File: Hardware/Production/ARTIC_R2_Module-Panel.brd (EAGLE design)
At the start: 154.2 x 147.3 mm, 2846 parts, among them J101 U.FL, J126 U.FL, J151 U.FL, J176 U.FL, J201 U.FL, J226 U.FL, J25 U.FL, J251 U.FL, J26 U.FL, J276 U.FL, J301 U.FL, J326 U.FL, J351 U.FL, J376 U.FL, J401 U.FL, J426 U.FL, J451 U.FL, J476 U.FL, J51 U.FL, J76 U.FL, K1 TLP3475R, K10 TLP3475R, K11 TLP3475R, K12 TLP3475R, K13 TLP3475R, K14 TLP3475R, K15 TLP3475R, K16 TLP3475R, K17 TLP3475R, K18 TLP3475R, K19 TLP3475R, K2 TLP3475R, K20 TLP3475R, K3 TLP3475R, K4 TLP3475R, K5 TLP3475R, K6 TLP3475R, K7 TLP3475R, K8 TLP3475R, K9 TLP3475R, Q1 5.8A/30V/35mΩ, Q10 5.8A/30V/35mΩ, Q11 5.8A/30V/35mΩ, Q12 5.8A/30V/35mΩ, Q13 5.8A/30V/35mΩ, Q14 5.8A/30V/35mΩ, Q15 5.8A/30V/35mΩ, Q16 5.8A/30V/35mΩ, Q17 5.8A/30V/35mΩ, Q18 5.8A/30V/35mΩ, Q19 5.8A/30V/35mΩ, Q2 5.8A/30V/35mΩ, Q20 5.8A/30V/35mΩ, Q3 5.8A/30V/35mΩ, Q4 5.8A/30V/35mΩ, Q5 5.8A/30V/35mΩ, Q6 5.8A/30V/35mΩ, Q7 5.8A/30V/35mΩ, Q8 5.8A/30V/35mΩ, Q9 5.8A/30V/35mΩ, U1 ADM4210-1, U10 1.8V/100mA, U100 1.8V/100mA, U101 3.0V, U102 ADM4210-1, U103 ARTIC_R2, U104 RFPA0133, U105 AS179-92LF, U106 1.8V/100mA, U107 3.0V, U108 ADM4210-1, U109 ARTIC_R2, U11 3.0V, U110 RFPA0133, U111 AS179-92LF, U112 1.8V/100mA, U113 3.0V, U114 ADM4210-1, U115 ARTIC_R2, U116 RFPA0133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

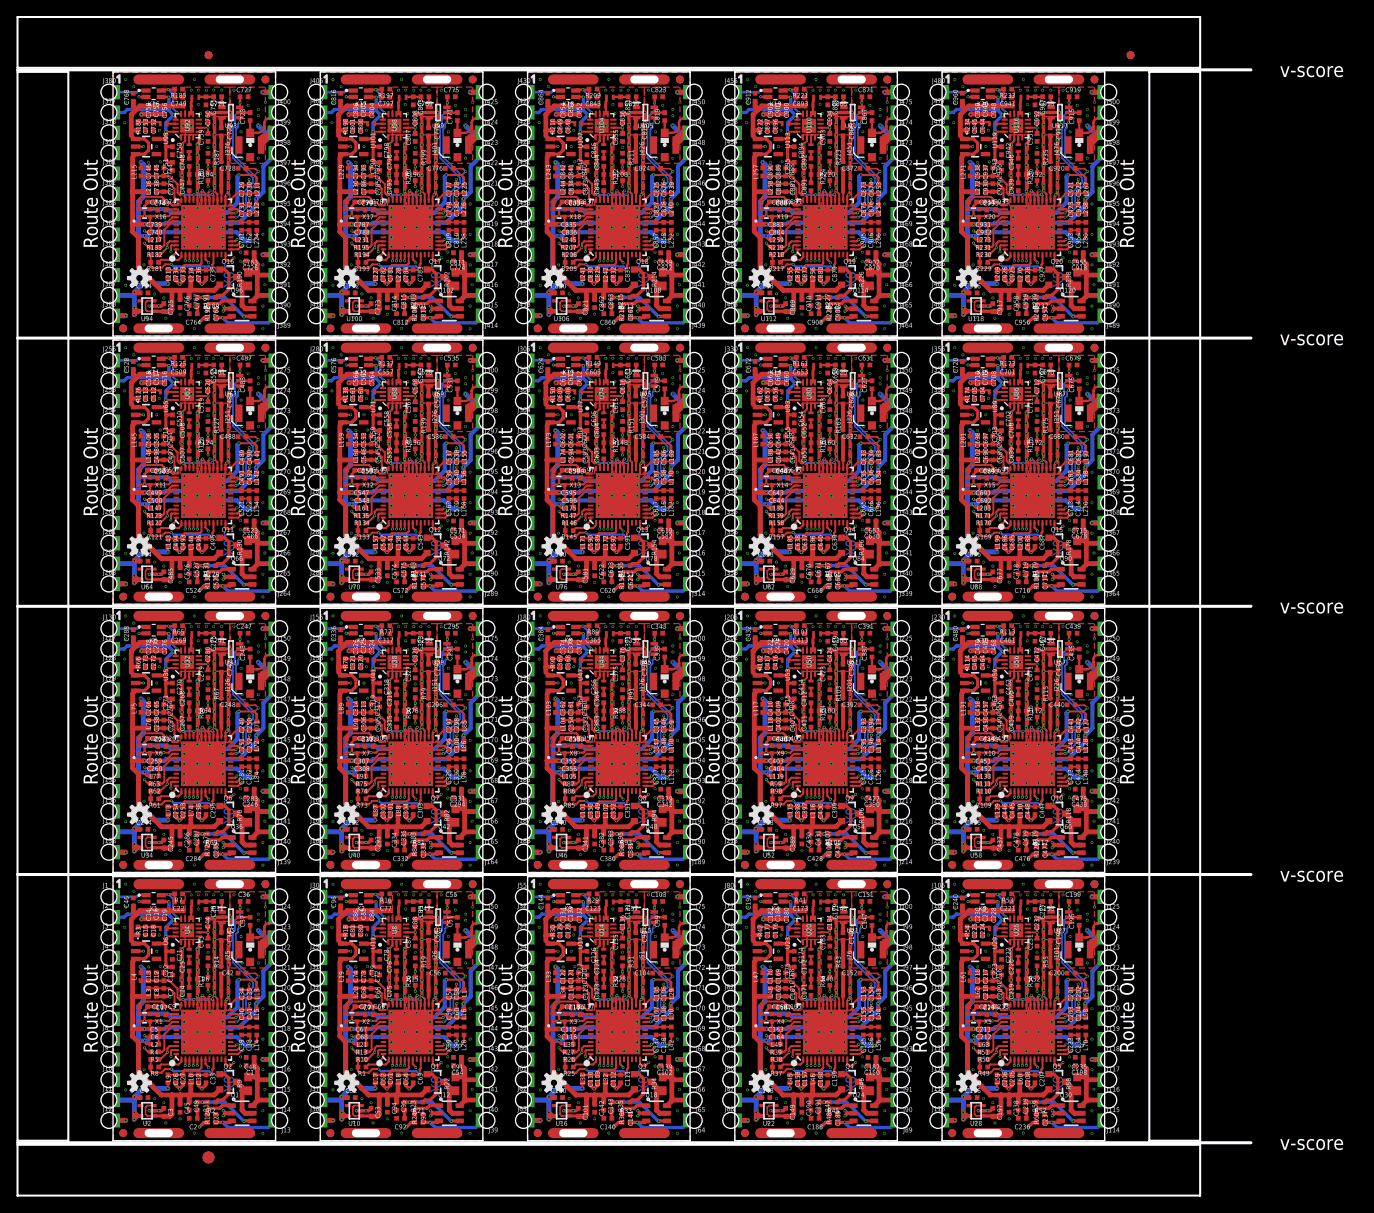
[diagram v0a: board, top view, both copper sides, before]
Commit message: Added the flash memory in USON format
The flash has its own power pin so it can be programmed independantly - without needing the ARTIC to be powered up and held in reset. The user will need to jump the flash power pad across to the adjacent VDD pad on their board.
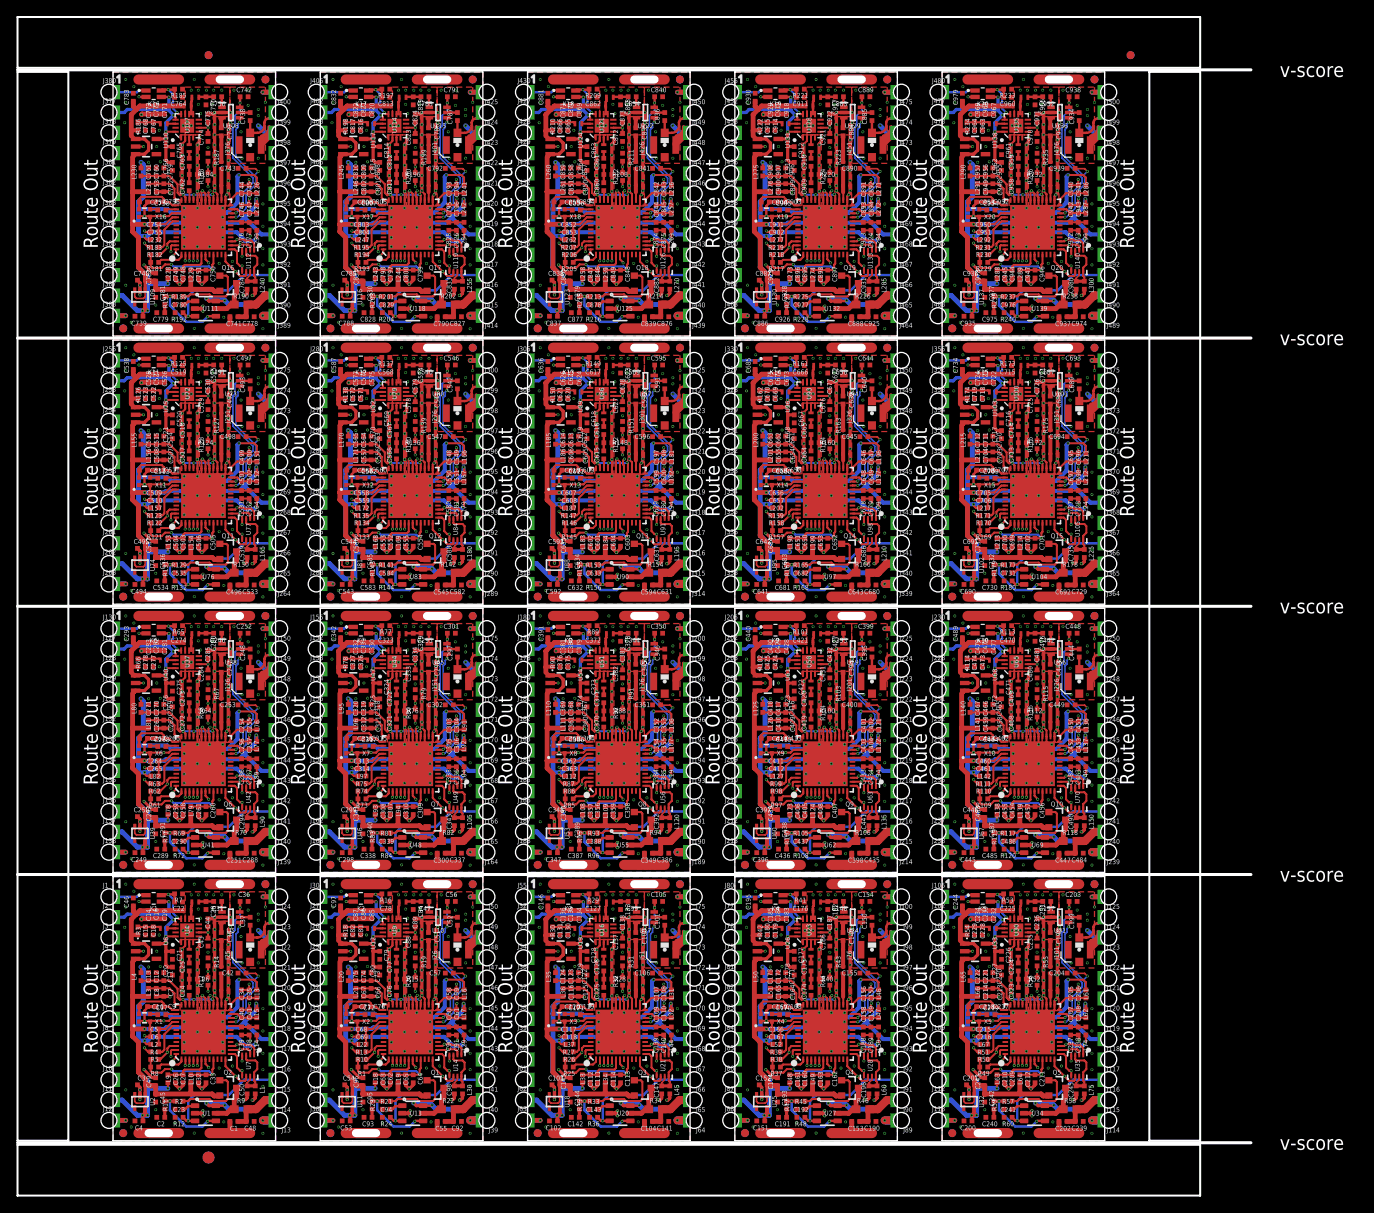
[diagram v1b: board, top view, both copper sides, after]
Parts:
- removed LOGO21, LOGO22, LOGO23, LOGO24, LOGO25, LOGO26, LOGO27, LOGO28, LOGO29, LOGO30, LOGO31, LOGO32, LOGO33, LOGO34, LOGO35, LOGO36, LOGO37, LOGO38, LOGO39, LOGO40: OSHW-LOGOS, SparkFun-Aesthetics:OSHW-LOGO-S
- added C961, C967, C970: 100pF, SparkFun-Capacitors:0402-TIGHT
- added C962, C964, C968, C971, C977: 2.2uF, SparkFun-Capacitors:0402-TIGHT
- added C963, C972: 22pF, SparkFun-Capacitors:0402-TIGHT
- added C965: 2.4 pF, SparkFun-Capacitors:0402_MURATA
- added C966: 9.1pF, New_Parts_Capacitors:0402-TIGHT
- added C969: 10uF, SparkFun-Capacitors:0402-TIGHT
- added C973, C974, C978, C980: 0.1uF, SparkFun-Capacitors:0402-TIGHT
- added C975: 10nF, SparkFun-Capacitors:0402-TIGHT
- added C976, C979: 1.0uF, SparkFun-Capacitors:0402-TIGHT
- added L281, L296: 12nH, New_Parts_Coils:0402_COILCRAFT
- added L282, L297: 30nH, New_Parts_Coils:0402_COILCRAFT
- added L283, L298: 51nH, New_Parts_Coils:0402_COILCRAFT
- added L284, L285, L286, L287, L288, L289, L290, L291, L292, L299, L300: 30Ω, SparkFun-Coils:0402-TIGHT
- added L293: 18nH, New_Parts_Coils:0402_COILCRAFT
- added L294: 15nH, New_Parts_Coils:0402_COILCRAFT
- added L295: 27nH, New_Parts_Coils:0402_COILCRAFT
- added U121, U128, U135: RFPA0133, New_Parts_IC-Comms:QFN50P300X300X86-17N
- added U122, U129, U136: AS179-92LF, New_Parts_IC-Comms:SOT65P220X100-6N
- added U123, U130, U137: 1.8V/100mA, SparkFun-IC-Power:SC70
- added U124, U131, U138: 3.0V, New_Parts_IC-Power:SOT23-5
- added U125, U132, U139: ADM4210-1, New_Parts_IC-Power:TSOT6
- added U126, U133, U140: SST25VF020BUSON, New_Parts_IC-Memory:USON_3X2MM
- added U127, U134: ARTIC_R2, New_Parts_IC-Comms:QFN-48
- C100, C101, C148, C149, C197, C333, C477, C480, C52, C624, C645, C676, C693, C725, C73, C765, C813, C820, C841, C861, C869, C885, C889, C909, C912, C933, C960: value 1.0uF -> 100pF
- C102, C319, C342, C417, C486, C511, C54, C609, C613, C760, C805, C94, C952: value 2.2uF -> 1.0uF
- C103, C123, C146, C151, C152, C168, C172, C195, C200, C221, C241, C270, C290, C315, C339, C364, C391, C413, C440, C462, C535, C564, C584, C711, C756, C903, C936, C97: value 100pF -> 1.0uF
- C104, C135, C180, C193, C242, C276, C291, C327, C423, C481, C487, C530, C536, C55, C579, C625, C674, C723, C775, C817, C824, C866, C888, C913, C915, C919: value 100pF -> 2.2uF
- C105, C128, C137, C155, C176, C203, C224, C253, C272, C281, C297, C301, C345, C351, C393, C395, C399, C416, C443, C449, C491, C493, C497, C541, C547, C569, C57, C589, C591, C595, C617, C639, C665, C687, C689, C713, C737, C785, C787, C835, C857, C883, C921: value 22pF -> 100pF
- C106, C154, C186, C204, C235, C252, C302, C330, C346, C350, C379, C394, C400, C431, C442, C444, C448, C492, C498, C540, C542, C546, C575, C590, C596, C618, C638, C640, C644, C666, C667, C688, C714, C715, C736, C738, C762, C763, C786, C811, C834, C836, C863, C884, C906, C911, C932, C955, C959: value 0.1uF -> 100pF
- C117, C213, C237, C309, C313, C384, C405, C409, C501, C505, C580, C597, C601, C629, C669, C697, C793, C816: value 1.0uF -> 22pF
- C118, C214, C310, C406, C502, C598: value 47nF -> 0.1uF
- C119, C887, C935: value 1.0nF -> 1.0uF
- C120, C267, C316, C365, C414, C708, C855: value 100pF -> 47nF
- C121: value 1.0uF -> 1.0nF
- C122, C134, C422, C470, C518, C566, C710, C890, C938: value 10uF -> 100pF
- C124, C173, C222, C516, C577, C626, C663, C675, C75, C87, C871, C920: value 100pF -> 10uF
- C127, C150, C175, C177, C198, C223, C225, C232, C246, C273, C321, C367, C373, C382, C421, C465, C469, C517, C520, C526, C568, C616, C661, C664, C774, C79, C808, C814, C85, C862, C88, C910, C918, C958: value 2.2uF -> 100pF
- C130, C754, C850, C946: value 2.4 pF -> 22pF; device SparkFun-Capacitors:0402_MURATA -> SparkFun-Capacitors:0402-TIGHT
- C131, C227: value 9.1pF -> 2.2uF; device New_Parts_Capacitors:0402-TIGHT -> SparkFun-Capacitors:0402-TIGHT
- C132, C279, C769, C818, C867: value 100pF -> 2.4 pF; device SparkFun-Capacitors:0402-TIGHT -> SparkFun-Capacitors:0402_MURATA
- C133, C280, C574: value 2.2uF -> 9.1pF; device SparkFun-Capacitors:0402-TIGHT -> New_Parts_Capacitors:0402-TIGHT
- C136, C271, C369, C430, C565, C712, C822: value 2.2uF -> 10uF
- C138, C187, C202, C282, C300, C331, C383, C398, C474, C496, C523, C527, C570, C594, C619, C634, C692, C719, C732, C815, C830, C922, C928, C95: value 0.1uF -> 2.2uF
- C139, C156, C158, C160, C162, C164, C254, C256, C258, C260, C335, C352, C354, C356, C450, C452, C522, C548, C571, C58, C60, C62, C64, C66, C68, C767, C874, C90: value 0.1uF -> 22pF
- C140, C92: value 10nF -> 0.1uF
- C141, C165, C189, C196, C245, C261, C265, C288, C292, C336, C341, C357, C361, C453, C457, C484, C532, C533, C549, C553, C581, C649, C69, C745, C96: value 1.0uF -> 0.1uF
- C142, C534: value 2.2uF -> 10nF
- C143, C250, C298, C348, C396, C446, C494, C538, C544, C592, C636, C642, C682, C690, C734, C740, C780, C788, C832, C858, C878, C907, C930: value 0.1uF -> 1.0uF
- C144, C285, C340, C389, C429, C432, C576, C621, C628, C677, C717, C741, C768, C772, C821, C864, C937: value 1.0uF -> 2.2uF
- C145, C147, C194, C216, C243, C312, C337, C343, C363, C385, C386, C392, C408, C412, C434, C435, C439, C459, C461, C483, C488, C50, C504, C508, C510, C555, C557, C600, C604, C606, C631, C651, C653, C679, C680, C696, C700, C702, C728, C747, C749, C796, C798, C804, C843, C845, C892, C894, C900, C941, C951, C98: value 100pF -> 0.1uF
- C153, C233, C251, C349, C425, C447, C521, C545, C585, C643, C683, C781, C80, C873, C879, C89: value 22pF -> 2.2uF
- C157, C159, C161, C163, C255, C257, C259, C353, C355, C441, C451, C537, C539, C59, C608, C61, C63, C635, C637, C65, C67, C704, C729, C733, C735, C777, C800, C827, C831, C833, C875, C896, C925, C929, C931: value 22pF -> 0.1uF
- C166, C262, C358, C454, C550, C646: value 47nF -> 22pF
- C167, C263, C359, C455, C551, C647: value 1.0nF -> 0.1uF
- C169: value 1.0uF -> 47nF
- C170, C758: value 10uF -> 1.0nF
- C178, C82: value 2.4 pF -> 2.2uF; device SparkFun-Capacitors:0402_MURATA -> SparkFun-Capacitors:0402-TIGHT
- C179, C803, C899: value 9.1pF -> 22pF; device New_Parts_Capacitors:0402-TIGHT -> SparkFun-Capacitors:0402-TIGHT
- C181, C328, C622: value 2.2uF -> 2.4 pF; device SparkFun-Capacitors:0402-TIGHT -> SparkFun-Capacitors:0402_MURATA
- C182: value 10uF -> 9.1pF; device SparkFun-Capacitors:0402-TIGHT -> New_Parts_Capacitors:0402-TIGHT
- C185, C320, C761: value 22pF -> 10uF
- C188, C620: value 10nF -> 22pF
- C190, C238, C294, C390, C559, C582, C630, C655, C657, C751, C753, C847, C849, C853, C943, C945, C949: value 2.2uF -> 0.1uF
- C191, C730, C828, C926: value 0.1uF -> 10nF
- C201, C249, C299, C347, C368, C397, C445, C489, C495, C543, C560, C587, C593, C633, C641, C685, C691, C731, C739, C783, C809, C829, C881, C927: value 22pF -> 1.0uF
- C215, C311, C407, C503, C599, C695: value 1.0nF -> 22pF
- C218, C806: value 10uF -> 47nF
- C219, C268, C317, C366, C660, C72, C807: value 100pF -> 1.0nF
- C226, C274, C322, C370, C514: value 2.4 pF -> 100pF; device SparkFun-Capacitors:0402_MURATA -> SparkFun-Capacitors:0402-TIGHT
- C228, C264, C360, C375, C411, C433, C456, C460, C482, C507, C509, C531, C552, C556, C558, C603, C605, C648, C652, C654, C699, C701, C727, C744, C748, C750, C776, C795, C797, C844, C846, C852, C865, C891, C893, C914, C940, C942, C948: value 100pF -> 22pF
- C230: value 10uF -> 2.4 pF; device SparkFun-Capacitors:0402-TIGHT -> SparkFun-Capacitors:0402_MURATA
- C231, C721, C770, C819, C84: value 100pF -> 9.1pF; device SparkFun-Capacitors:0402-TIGHT -> New_Parts_Capacitors:0402-TIGHT
- C234, C283, C479, C810, C859: value 0.1uF -> 10uF
- C236, C380, C572, C668: value 10nF -> 2.2uF
- C240, C436, C485, C93: value 1.0uF -> 10nF
- C266, C662, C74, C854: value 10uF -> 1.0uF
- C275, C323, C371, C419, C563: value 9.1pF -> 100pF; device New_Parts_Capacitors:0402-TIGHT -> SparkFun-Capacitors:0402-TIGHT
- C277, C286, C424, C607, C678, C703, C705, C718, C799, C801, C81, C895, C897, C901: value 2.2uF -> 22pF
- C278, C374, C86: value 10uF -> 2.2uF
- C284, C428, C716, C764, C812, C860: value 10nF -> 100pF
- C289, C338, C387, C583, C632: value 100pF -> 10nF
- C314, C410, C506, C602, C698, C794, C902: value 10uF -> 0.1uF
- C326, C362, C458, C554, C650, C746, C842, C950: value 10uF -> 22pF
- C329: value 22pF -> 9.1pF; device SparkFun-Capacitors:0402-TIGHT -> New_Parts_Capacitors:0402-TIGHT
- C332, C908: value 10nF -> 10uF
- C377: value 22pF -> 2.4 pF; device SparkFun-Capacitors:0402-TIGHT -> SparkFun-Capacitors:0402_MURATA
- C378, C427, C623: value 0.1uF -> 9.1pF; device SparkFun-Capacitors:0402-TIGHT -> New_Parts_Capacitors:0402-TIGHT
- C381, C528, C724, C773, C957: value 1.0uF -> 10uF
- C415, C513, C709, C856: value 2.2uF -> 1.0nF
- C418: value 2.4 pF -> 10uF; device SparkFun-Capacitors:0402_MURATA -> SparkFun-Capacitors:0402-TIGHT
- C426, C475, C671: value 0.1uF -> 2.4 pF; device SparkFun-Capacitors:0402-TIGHT -> SparkFun-Capacitors:0402_MURATA
- C463, C561, C757, C904: value 2.2uF -> 47nF
- C464, C905: value 22pF -> 1.0nF
- C466, C658: value 2.4 pF -> 1.0uF; device SparkFun-Capacitors:0402_MURATA -> SparkFun-Capacitors:0402-TIGHT
- C467: value 9.1pF -> 10uF; device New_Parts_Capacitors:0402-TIGHT -> SparkFun-Capacitors:0402-TIGHT
- C476: value 10nF -> 9.1pF; device SparkFun-Capacitors:0402-TIGHT -> New_Parts_Capacitors:0402-TIGHT
- C512, C953: value 22pF -> 47nF
- C515, C707: value 9.1pF -> 1.0uF; device New_Parts_Capacitors:0402-TIGHT -> SparkFun-Capacitors:0402-TIGHT
- C524: value 10nF -> 2.4 pF; device SparkFun-Capacitors:0402-TIGHT -> SparkFun-Capacitors:0402_MURATA
- C525, C672, C868, C917: value 1.0uF -> 9.1pF; device SparkFun-Capacitors:0402-TIGHT -> New_Parts_Capacitors:0402-TIGHT
- C562: value 2.4 pF -> 1.0nF; device SparkFun-Capacitors:0402_MURATA -> SparkFun-Capacitors:0402-TIGHT
- C573, C720, C916: value 1.0uF -> 2.4 pF; device SparkFun-Capacitors:0402-TIGHT -> SparkFun-Capacitors:0402_MURATA
- C610: value 2.4 pF -> 47nF; device SparkFun-Capacitors:0402_MURATA -> SparkFun-Capacitors:0402-TIGHT
- C611: value 9.1pF -> 1.0nF; device New_Parts_Capacitors:0402-TIGHT -> SparkFun-Capacitors:0402-TIGHT
- C659: value 9.1pF -> 47nF; device New_Parts_Capacitors:0402-TIGHT -> SparkFun-Capacitors:0402-TIGHT
- C681, C779, C877: value 22pF -> 10nF
- C694, C742, C934: value 47nF -> 100pF
- C70, C838, C886: value 47nF -> 1.0uF
- C706, C802, C898: value 2.4 pF -> 0.1uF; device SparkFun-Capacitors:0402_MURATA -> SparkFun-Capacitors:0402-TIGHT
- C71: value 1.0nF -> 47nF
- C743, C791: value 1.0nF -> 100pF
- C755, C851, C947: value 9.1pF -> 0.1uF; device New_Parts_Capacitors:0402-TIGHT -> SparkFun-Capacitors:0402-TIGHT
- C790: value 47nF -> 2.2uF
- C83: value 9.1pF -> 2.4 pF; device New_Parts_Capacitors:0402-TIGHT -> SparkFun-Capacitors:0402_MURATA
- C839: value 1.0nF -> 2.2uF
- C954: value 0.1uF -> 1.0nF
- C956: value 10nF -> 1.0uF
- L100, L115, L130, L145, L160, L175, L280, L70, L85: value 30Ω -> 27nH; device SparkFun-Coils:0402-TIGHT -> New_Parts_Coils:0402_COILCRAFT
- L101, L116, L131, L146, L161, L266, L56, L71, L86: value 30Ω -> 12nH; device SparkFun-Coils:0402-TIGHT -> New_Parts_Coils:0402_COILCRAFT
- L102, L117, L132, L147, L252, L267, L42, L57, L72, L87: value 30Ω -> 30nH; device SparkFun-Coils:0402-TIGHT -> New_Parts_Coils:0402_COILCRAFT
- L103, L118, L133, L238, L253, L268, L28, L43, L58, L73, L88: value 30Ω -> 51nH; device SparkFun-Coils:0402-TIGHT -> New_Parts_Coils:0402_COILCRAFT
- L106, L120, L134, L22, L232, L246, L260, L274, L36, L50, L64, L78, L92: value 18nH -> 30Ω; device New_Parts_Coils:0402_COILCRAFT -> SparkFun-Coils:0402-TIGHT
- L107, L121, L135, L149, L247, L261, L275, L37, L51, L65, L79, L93: value 15nH -> 30Ω; device New_Parts_Coils:0402_COILCRAFT -> SparkFun-Coils:0402-TIGHT
- L108, L122, L136, L150, L164, L262, L276, L52, L66, L80, L94: value 27nH -> 30Ω; device New_Parts_Coils:0402_COILCRAFT -> SparkFun-Coils:0402-TIGHT
- L109, L123, L137, L151, L165, L179, L277, L67, L81, L95: value 12nH -> 30Ω; device New_Parts_Coils:0402_COILCRAFT -> SparkFun-Coils:0402-TIGHT
- L110, L124, L138, L152, L166, L180, L194, L82, L96: value 30nH -> 30Ω; device New_Parts_Coils:0402_COILCRAFT -> SparkFun-Coils:0402-TIGHT
- L111, L125, L139, L153, L167, L181, L195, L209, L97: value 51nH -> 30Ω; device New_Parts_Coils:0402_COILCRAFT -> SparkFun-Coils:0402-TIGHT
- L113, L128, L143, L158, L173, L188, L203, L98: value 30Ω -> 18nH; device SparkFun-Coils:0402-TIGHT -> New_Parts_Coils:0402_COILCRAFT
- L114, L129, L144, L159, L174, L189, L84, L99: value 30Ω -> 15nH; device SparkFun-Coils:0402-TIGHT -> New_Parts_Coils:0402_COILCRAFT
- L148: value 18nH -> 51nH
- L162: value 18nH -> 30nH
- L163: value 15nH -> 51nH
- L176: value 18nH -> 12nH
- L177: value 15nH -> 30nH
- L178: value 27nH -> 51nH
- L190: value 18nH -> 27nH
- L191: value 15nH -> 12nH
- L192: value 27nH -> 30nH
- L193: value 12nH -> 51nH
- L204: value 18nH -> 15nH
- L205: value 15nH -> 27nH
- L206: value 27nH -> 12nH
- L207: value 12nH -> 30nH
- L208: value 30nH -> 51nH
- L23, L233: value 15nH -> 18nH
- L234, L24: value 27nH -> 15nH
- L235, L25: value 12nH -> 27nH
- L236, L26: value 30nH -> 12nH
- L237, L27: value 51nH -> 30nH
- L248, L38: value 27nH -> 18nH
- L249, L39: value 12nH -> 15nH
- L250, L40: value 30nH -> 27nH
- L251, L41: value 51nH -> 12nH
- L263, L53: value 12nH -> 18nH
- L264, L54: value 30nH -> 15nH
- L265, L55: value 51nH -> 27nH
- L278, L68: value 30nH -> 18nH
- L279, L69: value 51nH -> 15nH
- L83: value 51nH -> 18nH
- U$100, U$126, U$152, U$178, U$204, U$230, U$256, U$282, U$308, U$334, U$360, U$386, U$412, U$438, U$464, U$48, U$490, U$516, U$74: device output:#SCLK#0 -> output:#COPI#0
- U$101, U$127, U$153, U$179, U$205, U$231, U$257, U$283, U$309, U$335, U$361, U$387, U$413, U$439, U$465, U$49, U$491, U$517, U$75: device output:#COPI#0 -> output:#CIPO#0
- U$102, U$128, U$154, U$180, U$206, U$232, U$258, U$284, U$310, U$336, U$362, U$388, U$414, U$440, U$466, U$492, U$50, U$518, U$76: device output:#CIPO#0 -> output:#1#8V_OUT#0
- U$103, U$129, U$155, U$181, U$207, U$233, U$259, U$285, U$311, U$337, U$363, U$389, U$415, U$441, U$467, U$493, U$51, U$519, U$77: device output:#1#8V_OUT#0 -> output:ARTIC_R20
- U$104, U$130, U$156, U$182, U$208, U$234, U$260, U$286, U$312, U$338, U$364, U$390, U$416, U$442, U$468, U$494, U$52, U$520, U$78: device output:ARTIC_R20 -> output:#FLASH_PWR#0
- U$112, U$138, U$164, U$190, U$216, U$242, U$268, U$294, U$320, U$34, U$346, U$372, U$398, U$424, U$450, U$476, U$502, U$60, U$86: device output:#VIN#0 -> output:#FLSH_SCLK#0
- U$113, U$139, U$165, U$191, U$217, U$243, U$269, U$295, U$321, U$347, U$35, U$373, U$399, U$425, U$451, U$477, U$503, U$61, U$87: device output:#FLSH_SCLK#0 -> output:#FLSH_SI#0
- U$114, U$140, U$166, U$192, U$218, U$244, U$270, U$296, U$322, U$348, U$36, U$374, U$400, U$426, U$452, U$478, U$504, U$62, U$88: device output:#FLSH_SI#0 -> output:#FLSH_CEN#0
- U$115, U$141, U$167, U$193, U$219, U$245, U$271, U$297, U$323, U$349, U$37, U$375, U$401, U$427, U$453, U$479, U$505, U$63, U$89: device output:#FLSH_CEN#0 -> output:#FLSH_SO#0
- U$116, U$142, U$168, U$194, U$220, U$246, U$272, U$298, U$324, U$350, U$376, U$38, U$402, U$428, U$454, U$480, U$506, U$64, U$90: device output:#FLSH_SO#0 -> output:#3#3V_OUT#0
- U$117, U$143, U$169, U$195, U$221, U$247, U$273, U$299, U$325, U$351, U$377, U$39, U$403, U$429, U$455, U$481, U$507, U$65, U$91: device output:#3#3V_OUT#0 -> output:#ANTENNA#0
- U$118, U$144, U$170, U$196, U$222, U$248, U$274, U$300, U$326, U$352, U$378, U$40, U$404, U$430, U$456, U$482, U$508, U$66, U$92: device output:#ANTENNA#0 -> output:#G8#0
- U$119, U$145, U$171, U$197, U$223, U$249, U$275, U$301, U$327, U$353, U$379, U$405, U$41, U$431, U$457, U$483, U$509, U$67, U$93: device output:#G8#0 -> output:#3#0V_OUT#0
- U$120, U$146, U$172, U$198, U$224, U$250, U$276, U$302, U$328, U$354, U$380, U$406, U$42, U$432, U$458, U$484, U$510, U$68, U$94: device output:#3#0V_OUT#0 -> output:#BOOT#0
- U$121, U$147, U$173, U$199, U$225, U$251, U$277, U$303, U$329, U$355, U$381, U$407, U$43, U$433, U$459, U$485, U$511, U$69, U$95: device output:#BOOT#0 -> output:#INT1#0
- U$122, U$148, U$174, U$200, U$226, U$252, U$278, U$304, U$330, U$356, U$382, U$408, U$434, U$44, U$460, U$486, U$512, U$70, U$96: device output:#INT1#0 -> output:#INT2#0
- U$123, U$149, U$175, U$201, U$227, U$253, U$279, U$305, U$331, U$357, U$383, U$409, U$435, U$45, U$461, U$487, U$513, U$71, U$97: device output:#INT2#0 -> output:#RESETB#0
- U$124, U$150, U$176, U$202, U$228, U$254, U$280, U$306, U$332, U$358, U$384, U$410, U$436, U$46, U$462, U$488, U$514, U$72, U$98: device output:#RESETB#0 -> output:#CS#0
- U$125, U$151, U$177, U$203, U$229, U$255, U$281, U$307, U$333, U$359, U$385, U$411, U$437, U$463, U$47, U$489, U$515, U$73, U$99: device output:#CS#0 -> output:#SCLK#0
- U$8: device output:#VIN#0 -> output:#FLASH_PWR#0
- U10, U52, U94: value 1.8V/100mA -> AS179-92LF; device SparkFun-IC-Power:SC70 -> New_Parts_IC-Comms:SOT65P220X100-6N
- U100, U16, U58: value 1.8V/100mA -> RFPA0133; device SparkFun-IC-Power:SC70 -> New_Parts_IC-Comms:QFN50P300X300X86-17N
- U101, U17, U59: value 3.0V -> AS179-92LF; device New_Parts_IC-Power:SOT23-5 -> New_Parts_IC-Comms:SOT65P220X100-6N
- U102, U18, U60: value ADM4210-1 -> 1.8V/100mA; device New_Parts_IC-Power:TSOT6 -> SparkFun-IC-Power:SC70
- U103, U19, U61: value ARTIC_R2 -> 3.0V; device New_Parts_IC-Comms:QFN-48 -> New_Parts_IC-Power:SOT23-5
- U104, U20, U62: value RFPA0133 -> ADM4210-1; device New_Parts_IC-Comms:QFN50P300X300X86-17N -> New_Parts_IC-Power:TSOT6
- U105, U21, U63: value AS179-92LF -> SST25VF020BUSON; device New_Parts_IC-Comms:SOT65P220X100-6N -> New_Parts_IC-Memory:USON_3X2MM
- U106, U22, U64: value 1.8V/100mA -> ARTIC_R2; device SparkFun-IC-Power:SC70 -> New_Parts_IC-Comms:QFN-48
- U107, U23, U65: value 3.0V -> RFPA0133; device New_Parts_IC-Power:SOT23-5 -> New_Parts_IC-Comms:QFN50P300X300X86-17N
- U108, U24, U66: value ADM4210-1 -> AS179-92LF; device New_Parts_IC-Power:TSOT6 -> New_Parts_IC-Comms:SOT65P220X100-6N
- U109, U25, U67: value ARTIC_R2 -> 1.8V/100mA; device New_Parts_IC-Comms:QFN-48 -> SparkFun-IC-Power:SC70
- U11, U53, U95: value 3.0V -> 1.8V/100mA; device New_Parts_IC-Power:SOT23-5 -> SparkFun-IC-Power:SC70
- U110, U26, U68: value RFPA0133 -> 3.0V; device New_Parts_IC-Comms:QFN50P300X300X86-17N -> New_Parts_IC-Power:SOT23-5
- U111, U27, U69: value AS179-92LF -> ADM4210-1; device New_Parts_IC-Comms:SOT65P220X100-6N -> New_Parts_IC-Power:TSOT6
- U112, U28, U70: value 1.8V/100mA -> SST25VF020BUSON; device SparkFun-IC-Power:SC70 -> New_Parts_IC-Memory:USON_3X2MM
- U113, U29, U71: value 3.0V -> ARTIC_R2; device New_Parts_IC-Power:SOT23-5 -> New_Parts_IC-Comms:QFN-48
- U114, U30, U72: value ADM4210-1 -> RFPA0133; device New_Parts_IC-Power:TSOT6 -> New_Parts_IC-Comms:QFN50P300X300X86-17N
- U115, U31, U73: value ARTIC_R2 -> AS179-92LF; device New_Parts_IC-Comms:QFN-48 -> New_Parts_IC-Comms:SOT65P220X100-6N
- U116, U32, U74: value RFPA0133 -> 1.8V/100mA; device New_Parts_IC-Comms:QFN50P300X300X86-17N -> SparkFun-IC-Power:SC70
- U117, U33, U75: value AS179-92LF -> 3.0V; device New_Parts_IC-Comms:SOT65P220X100-6N -> New_Parts_IC-Power:SOT23-5
- U118, U34, U76: value 1.8V/100mA -> ADM4210-1; device SparkFun-IC-Power:SC70 -> New_Parts_IC-Power:TSOT6
- U119, U35, U77: value 3.0V -> SST25VF020BUSON; device New_Parts_IC-Power:SOT23-5 -> New_Parts_IC-Memory:USON_3X2MM
- U12, U54, U96: value ADM4210-1 -> 3.0V; device New_Parts_IC-Power:TSOT6 -> New_Parts_IC-Power:SOT23-5
- U120, U36, U78: value ADM4210-1 -> ARTIC_R2; device New_Parts_IC-Power:TSOT6 -> New_Parts_IC-Comms:QFN-48
- U13, U55, U97: value ARTIC_R2 -> ADM4210-1; device New_Parts_IC-Comms:QFN-48 -> New_Parts_IC-Power:TSOT6
- U14, U56, U98: value RFPA0133 -> SST25VF020BUSON; device New_Parts_IC-Comms:QFN50P300X300X86-17N -> New_Parts_IC-Memory:USON_3X2MM
- U15, U57, U99: value AS179-92LF -> ARTIC_R2; device New_Parts_IC-Comms:SOT65P220X100-6N -> New_Parts_IC-Comms:QFN-48
- U37, U79: value ARTIC_R2 -> RFPA0133; device New_Parts_IC-Comms:QFN-48 -> New_Parts_IC-Comms:QFN50P300X300X86-17N
- U38, U80: value RFPA0133 -> AS179-92LF; device New_Parts_IC-Comms:QFN50P300X300X86-17N -> New_Parts_IC-Comms:SOT65P220X100-6N
- U39, U81: value AS179-92LF -> 1.8V/100mA; device New_Parts_IC-Comms:SOT65P220X100-6N -> SparkFun-IC-Power:SC70
- U40, U82: value 1.8V/100mA -> 3.0V; device SparkFun-IC-Power:SC70 -> New_Parts_IC-Power:SOT23-5
- U41, U83: value 3.0V -> ADM4210-1; device New_Parts_IC-Power:SOT23-5 -> New_Parts_IC-Power:TSOT6
- U42, U84: value ADM4210-1 -> SST25VF020BUSON; device New_Parts_IC-Power:TSOT6 -> New_Parts_IC-Memory:USON_3X2MM
- U49, U7, U91: value ARTIC_R2 -> SST25VF020BUSON; device New_Parts_IC-Comms:QFN-48 -> New_Parts_IC-Memory:USON_3X2MM
- U50, U8, U92: value RFPA0133 -> ARTIC_R2; device New_Parts_IC-Comms:QFN50P300X300X86-17N -> New_Parts_IC-Comms:QFN-48
- U51, U9, U93: value AS179-92LF -> RFPA0133; device New_Parts_IC-Comms:SOT65P220X100-6N -> New_Parts_IC-Comms:QFN50P300X300X86-17N
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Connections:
- new net FLASH_PWR: J16.1, L1.2
- new net FLASH_PWR1: J42.1, L30.2
- new net FLASH_PWR10: J267.1, L165.2
- new net FLASH_PWR11: J292.1, L180.2
- new net FLASH_PWR12: J317.1, L195.2
- new net FLASH_PWR13: J342.1, L210.2
- new net FLASH_PWR14: J367.1, L225.2
- new net FLASH_PWR15: J392.1, L240.2
- new net FLASH_PWR16: J417.1, L255.2
- new net FLASH_PWR17: J442.1, L270.2
- new net FLASH_PWR18: J467.1, L285.2
- new net FLASH_PWR19: J492.1, L300.2
- new net FLASH_PWR2: J67.1, L45.2
- new net FLASH_PWR3: J92.1, L60.2
- new net FLASH_PWR4: J117.1, L75.2
- new net FLASH_PWR5: J142.1, L90.2
- new net FLASH_PWR6: J167.1, L105.2
- new net FLASH_PWR7: J192.1, L120.2
- new net FLASH_PWR8: J217.1, L135.2
- new net FLASH_PWR9: J242.1, L150.2
- new net FLASH_VCC: C50.1, L1.1, U7.3, U7.7, U7.8
- new net FLASH_VCC1: C98.1, L30.1, U14.3, U14.7, U14.8
- new net FLASH_VCC10: C539.1, L165.1, U77.3, U77.7, U77.8
- new net FLASH_VCC11: C588.1, L180.1, U84.3, U84.7, U84.8
- new net FLASH_VCC12: C637.1, L195.1, U91.3, U91.7, U91.8
- new net FLASH_VCC13: C686.1, L210.1, U98.3, U98.7, U98.8
- new net FLASH_VCC14: C735.1, L225.1, U105.3, U105.7, U105.8
- new net FLASH_VCC15: C784.1, L240.1, U112.3, U112.7, U112.8
- new net FLASH_VCC16: C833.1, L255.1, U119.3, U119.7, U119.8
- new net FLASH_VCC17: C882.1, L270.1, U126.3, U126.7, U126.8
- new net FLASH_VCC18: C931.1, L285.1, U133.3, U133.7, U133.8
- new net FLASH_VCC19: C980.1, L300.1, U140.3, U140.7, U140.8
- new net FLASH_VCC2: C147.1, L45.1, U21.3, U21.7, U21.8
- new net FLASH_VCC3: C196.1, L60.1, U28.3, U28.7, U28.8
- new net FLASH_VCC4: C245.1, L75.1, U35.3, U35.7, U35.8
- new net FLASH_VCC5: C294.1, L90.1, U42.3, U42.7, U42.8
- new net FLASH_VCC6: C343.1, L105.1, U49.3, U49.7, U49.8
- new net FLASH_VCC7: C392.1, L120.1, U56.3, U56.7, U56.8
- new net FLASH_VCC8: C441.1, L135.1, U63.3, U63.7, U63.8
- new net FLASH_VCC9: C490.1, L150.1, U70.3, U70.7, U70.8
- net 1.8V1: now also C53.1, L16.2, L18.2, L20.2, L22.2, L29.2, U11.5; no longer C52.1, L1.2, L17.2, L19.2, L21.2, L28.2, U10.5
- net 1.8V10: now also C494.1, L151.2, L153.2, L155.2, L157.2, L164.2, U74.5; no longer C484.1, L141.2, L143.2, L145.2, L147.2, L154.2, U64.5
- net 1.8V11: now also C543.1, L166.2, L170.2, L172.2, L179.2, U81.5; no longer C532.1, L155.2, L157.2, L159.2, L161.2, U70.5
- net 1.8V12: now also C592.1, L181.2, L183.2, L185.2, L187.2, L194.2, U88.5; no longer C580.1, L169.2, L171.2, L173.2, L175.2, L182.2, U76.5
- net 1.8V13: now also C641.1, L198.2, L200.2, L202.2, L209.2, U95.5; no longer C628.1, L183.2, L185.2, L187.2, L189.2, U82.5
- net 1.8V14: now also C690.1, L211.2, L213.2, L215.2, L217.2, L224.2, U102.5; no longer C676.1, L197.2, L199.2, L201.2, L203.2, L210.2, U88.5
- net 1.8V15: now also C739.1, L226.2, L228.2, L230.2, L232.2, L239.2, U109.5; no longer C724.1, L211.2, L213.2, L215.2, L217.2, L224.2, U94.5
- net 1.8V16: now also C788.1, L241.2, L243.2, L245.2, L247.2, L254.2, U116.5; no longer C772.1, L225.2, L227.2, L229.2, L231.2, L238.2, U100.5
- net 1.8V17: now also C837.1, L256.2, L258.2, L260.2, L262.2, L269.2, U123.5; no longer C820.1, L239.2, L241.2, L243.2, L245.2, L252.2, U106.5
- net 1.8V18: now also C886.1, L271.2, L273.2, L275.2, L277.2, L284.2, U130.5; no longer C868.1, L253.2, L255.2, L257.2, L259.2, L266.2, U112.5
- net 1.8V19: now also C935.1, L286.2, L288.2, L290.2, L292.2, L299.2, U137.5; no longer C916.1, L267.2, L269.2, L271.2, L273.2, L280.2, U118.5
- net 1.8V2: now also C102.1, L37.2, L44.2, U18.5; no longer C100.1, L29.2, L42.2, U16.5
- net 1.8V3: now also C151.1, L46.2, L48.2, L50.2, L52.2, L59.2, U25.5; no longer C148.1, L43.2, L45.2, L47.2, L49.2, L56.2, U22.5
- net 1.8V4: now also C200.1, L65.2, L67.2, L74.2, U32.5; no longer C196.1, L57.2, L59.2, L70.2, U28.5
- net 1.8V5: now also C249.1, L76.2, L78.2, L80.2, L82.2, L89.2, U39.5; no longer C244.1, L71.2, L73.2, L75.2, L77.2, L84.2, U34.5
- net 1.8V6: now also C298.1, L104.2, L93.2, L95.2, L97.2, U46.5; no longer C292.1, L85.2, L87.2, L89.2, L98.2, U40.5
- net 1.8V7: now also C347.1, L106.2, L108.2, L110.2, L119.2, U53.5; no longer C340.1, L101.2, L103.2, L105.2, L99.2, U46.5
- net 1.8V8: now also C396.1, L121.2, L123.2, L125.2, L127.2, L134.2, U60.5; no longer C388.1, L113.2, L115.2, L117.2, L119.2, L126.2, U52.5
- net 1.8V9: now also C445.1, L136.2, L138.2, L142.2, L149.2, U67.5; no longer C436.1, L127.2, L129.2, L131.2, L133.2, U58.5
- net ANTENNA1: now also C52.1; no longer C51.1
- net ANTENNA10: now also C493.1; no longer C483.1
- net ANTENNA11: now also C542.1; no longer C531.1
- net ANTENNA12: now also C591.1; no longer C579.1
- net ANTENNA13: now also C640.1; no longer C627.1
- net ANTENNA14: now also C689.1; no longer C675.1
- net ANTENNA15: now also C738.1; no longer C723.1
- net ANTENNA16: now also C787.1; no longer C771.1
- net ANTENNA17: now also C836.1; no longer C819.1
- net ANTENNA18: now also C885.1; no longer C867.1
- net ANTENNA19: now also C934.1; no longer C915.1
- net ANTENNA2: now also C101.1; no longer C99.1
- net ANTENNA3: now also C150.1; no longer C147.1
- net ANTENNA4: now also C199.1; no longer C195.1
- net ANTENNA5: now also C248.1; no longer C243.1
- net ANTENNA6: now also C297.1; no longer C291.1
- net ANTENNA7: now also C346.1; no longer C339.1
- net ANTENNA8: now also C395.1; no longer C387.1
- net ANTENNA9: now also C444.1; no longer C435.1
- net BOOT1: now also U8.46; no longer U7.46
- net BOOT10: now also U71.46; no longer U61.46
- net BOOT11: now also U78.46; no longer U67.46
- net BOOT12: now also U85.46; no longer U73.46
- net BOOT13: now also U92.46; no longer U79.46
- net BOOT14: now also U99.46; no longer U85.46
- net BOOT15: now also U106.46; no longer U91.46
- net BOOT16: now also U113.46; no longer U97.46
- net BOOT17: now also U120.46; no longer U103.46
- net BOOT18: now also U127.46; no longer U109.46
- net BOOT19: now also U134.46; no longer U115.46
- net BOOT2: now also U15.46; no longer U13.46
- net BOOT3: now also U22.46; no longer U19.46
- net BOOT4: now also U29.46; no longer U25.46
- net BOOT5: now also U36.46; no longer U31.46
- net BOOT6: now also U43.46; no longer U37.46
- net BOOT7: now also U50.46; no longer U43.46
- net BOOT8: now also U57.46; no longer U49.46
- net BOOT9: now also U64.46; no longer U55.46
- net CIPO1: now also U8.5; no longer U7.5
- net CIPO10: now also U71.5; no longer U61.5
- net CIPO11: now also U78.5; no longer U67.5
- net CIPO12: now also U85.5; no longer U73.5
- net CIPO13: now also U92.5; no longer U79.5
- net CIPO14: now also U99.5; no longer U85.5
- net CIPO15: now also U106.5; no longer U91.5
- net CIPO16: now also U113.5; no longer U97.5
- net CIPO17: now also U120.5; no longer U103.5
- net CIPO18: now also U127.5; no longer U109.5
- net CIPO19: now also U134.5; no longer U115.5
- net CIPO2: now also U15.5; no longer U13.5
- net CIPO3: now also U22.5; no longer U19.5
- net CIPO4: now also U29.5; no longer U25.5
- net CIPO5: now also U36.5; no longer U31.5
- net CIPO6: now also U43.5; no longer U37.5
- net CIPO7: now also U50.5; no longer U43.5
- net CIPO8: now also U57.5; no longer U49.5
- net CIPO9: now also U64.5; no longer U55.5
- net COPI1: now also U8.4; no longer U7.4
- net COPI10: now also U71.4; no longer U61.4
- net COPI11: now also U78.4; no longer U67.4
- net COPI12: now also U85.4; no longer U73.4
- net COPI13: now also U92.4; no longer U79.4
- net COPI14: now also U99.4; no longer U85.4
- net COPI15: now also U106.4; no longer U91.4
- net COPI16: now also U113.4; no longer U97.4
- net COPI17: now also U120.4; no longer U103.4
- net COPI18: now also U127.4; no longer U109.4
- net COPI19: now also U134.4; no longer U115.4
- net COPI2: now also U15.4; no longer U13.4
- net COPI3: now also U22.4; no longer U19.4
- net COPI4: now also U29.4; no longer U25.4
- net COPI5: now also U36.4; no longer U31.4
- net COPI6: now also U43.4; no longer U37.4
- net COPI7: now also U50.4; no longer U43.4
- net COPI8: now also U57.4; no longer U49.4
- net COPI9: now also U64.4; no longer U55.4
- net CS1: now also U8.2; no longer U7.2
- net CS10: now also U71.2; no longer U61.2
- net CS11: now also U78.2; no longer U67.2
- net CS12: now also U85.2; no longer U73.2
- net CS13: now also U92.2; no longer U79.2
- net CS14: now also U99.2; no longer U85.2
- net CS15: now also U106.2; no longer U91.2
- net CS16: now also U113.2; no longer U97.2
- net CS17: now also U120.2; no longer U103.2
- net CS18: now also U127.2; no longer U109.2
- net CS19: now also U134.2; no longer U115.2
- net CS2: now also U15.2; no longer U13.2
- net CS3: now also U22.2; no longer U19.2
- net CS4: now also U29.2; no longer U25.2
- net CS5: now also U36.2; no longer U31.2
- net CS6: now also U43.2; no longer U37.2
- net CS7: now also U50.2; no longer U43.2
- net CS8: now also U57.2; no longer U49.2
- net CS9: now also U64.2; no longer U55.2
- net FLSH_CEN: now also J21.1, U7.1; no longer J20.1
- net FLSH_CEN1: now also J47.1, U14.1, U8.15; no longer J46.1, U7.15
- net FLSH_CEN10: now also J272.1, U71.15, U77.1; no longer J271.1, U61.15
- net FLSH_CEN11: now also J297.1, U78.15, U84.1; no longer J296.1, U67.15
- net FLSH_CEN12: now also J322.1, U85.15, U91.1; no longer J321.1, U73.15
- net FLSH_CEN13: now also J347.1, U92.15, U98.1; no longer J346.1, U79.15
- net FLSH_CEN14: now also J372.1, U105.1, U99.15; no longer J371.1, U85.15
- net FLSH_CEN15: now also J397.1, U106.15, U112.1; no longer J396.1, U91.15
- net FLSH_CEN16: now also J422.1, U113.15, U119.1; no longer J421.1, U97.15
- net FLSH_CEN17: now also J447.1, U120.15, U126.1; no longer J446.1, U103.15
- net FLSH_CEN18: now also J472.1, U127.15, U133.1; no longer J471.1, U109.15
- net FLSH_CEN19: now also J497.1, U134.15, U140.1; no longer J496.1, U115.15
- net FLSH_CEN2: now also J72.1, U15.15, U21.1; no longer J71.1, U13.15
- net FLSH_CEN3: now also J97.1, U22.15, U28.1; no longer J96.1, U19.15
- net FLSH_CEN4: now also J122.1, U29.15, U35.1; no longer J121.1, U25.15
- net FLSH_CEN5: now also J147.1, U36.15, U42.1; no longer J146.1, U31.15
- net FLSH_CEN6: now also J172.1, U43.15, U49.1; no longer J171.1, U37.15
- net FLSH_CEN7: now also J197.1, U50.15, U56.1; no longer J196.1, U43.15
- net FLSH_CEN8: now also J222.1, U57.15, U63.1; no longer J221.1, U49.15
- net FLSH_CEN9: now also J247.1, U64.15, U70.1; no longer J246.1, U55.15
- net FLSH_SCLK: now also J18.1, U7.6; no longer J17.1
- net FLSH_SCLK1: now also J44.1, U14.6, U8.12; no longer J43.1, U7.12
- net FLSH_SCLK10: now also J269.1, U71.12, U77.6; no longer J268.1, U61.12
- net FLSH_SCLK11: now also J294.1, U78.12, U84.6; no longer J293.1, U67.12
- net FLSH_SCLK12: now also J319.1, U85.12, U91.6; no longer J318.1, U73.12
- net FLSH_SCLK13: now also J344.1, U92.12, U98.6; no longer J343.1, U79.12
- net FLSH_SCLK14: now also J369.1, U105.6, U99.12; no longer J368.1, U85.12
- net FLSH_SCLK15: now also J394.1, U106.12, U112.6; no longer J393.1, U91.12
- net FLSH_SCLK16: now also J419.1, U113.12, U119.6; no longer J418.1, U97.12
- net FLSH_SCLK17: now also J444.1, U120.12, U126.6; no longer J443.1, U103.12
- net FLSH_SCLK18: now also J469.1, U127.12, U133.6; no longer J468.1, U109.12
- net FLSH_SCLK19: now also J494.1, U134.12, U140.6; no longer J493.1, U115.12
- net FLSH_SCLK2: now also J69.1, U15.12, U21.6; no longer J68.1, U13.12
- net FLSH_SCLK3: now also J94.1, U22.12, U28.6; no longer J93.1, U19.12
- net FLSH_SCLK4: now also J119.1, U29.12, U35.6; no longer J118.1, U25.12
- net FLSH_SCLK5: now also J144.1, U36.12, U42.6; no longer J143.1, U31.12
- net FLSH_SCLK6: now also J169.1, U43.12, U49.6; no longer J168.1, U37.12
- net FLSH_SCLK7: now also J194.1, U50.12, U56.6; no longer J193.1, U43.12
- net FLSH_SCLK8: now also J219.1, U57.12, U63.6; no longer J218.1, U49.12
- net FLSH_SCLK9: now also J244.1, U64.12, U70.6; no longer J243.1, U55.12
- net FLSH_SI: now also J19.1, U7.5; no longer J18.1
- net FLSH_SI1: now also J45.1, U14.5, U8.13; no longer J44.1, U7.13
- net FLSH_SI10: now also J270.1, U71.13, U77.5; no longer J269.1, U61.13
- net FLSH_SI11: now also J295.1, U78.13, U84.5; no longer J294.1, U67.13
- net FLSH_SI12: now also J320.1, U85.13, U91.5; no longer J319.1, U73.13
- net FLSH_SI13: now also J345.1, U92.13, U98.5; no longer J344.1, U79.13
- net FLSH_SI14: now also J370.1, U105.5, U99.13; no longer J369.1, U85.13
- net FLSH_SI15: now also J395.1, U106.13, U112.5; no longer J394.1, U91.13
- net FLSH_SI16: now also J420.1, U113.13, U119.5; no longer J419.1, U97.13
- net FLSH_SI17: now also J445.1, U120.13, U126.5; no longer J444.1, U103.13
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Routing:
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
